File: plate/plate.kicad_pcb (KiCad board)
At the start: 2 copper layers, 134.1 x 128.8 mm, 4 parts

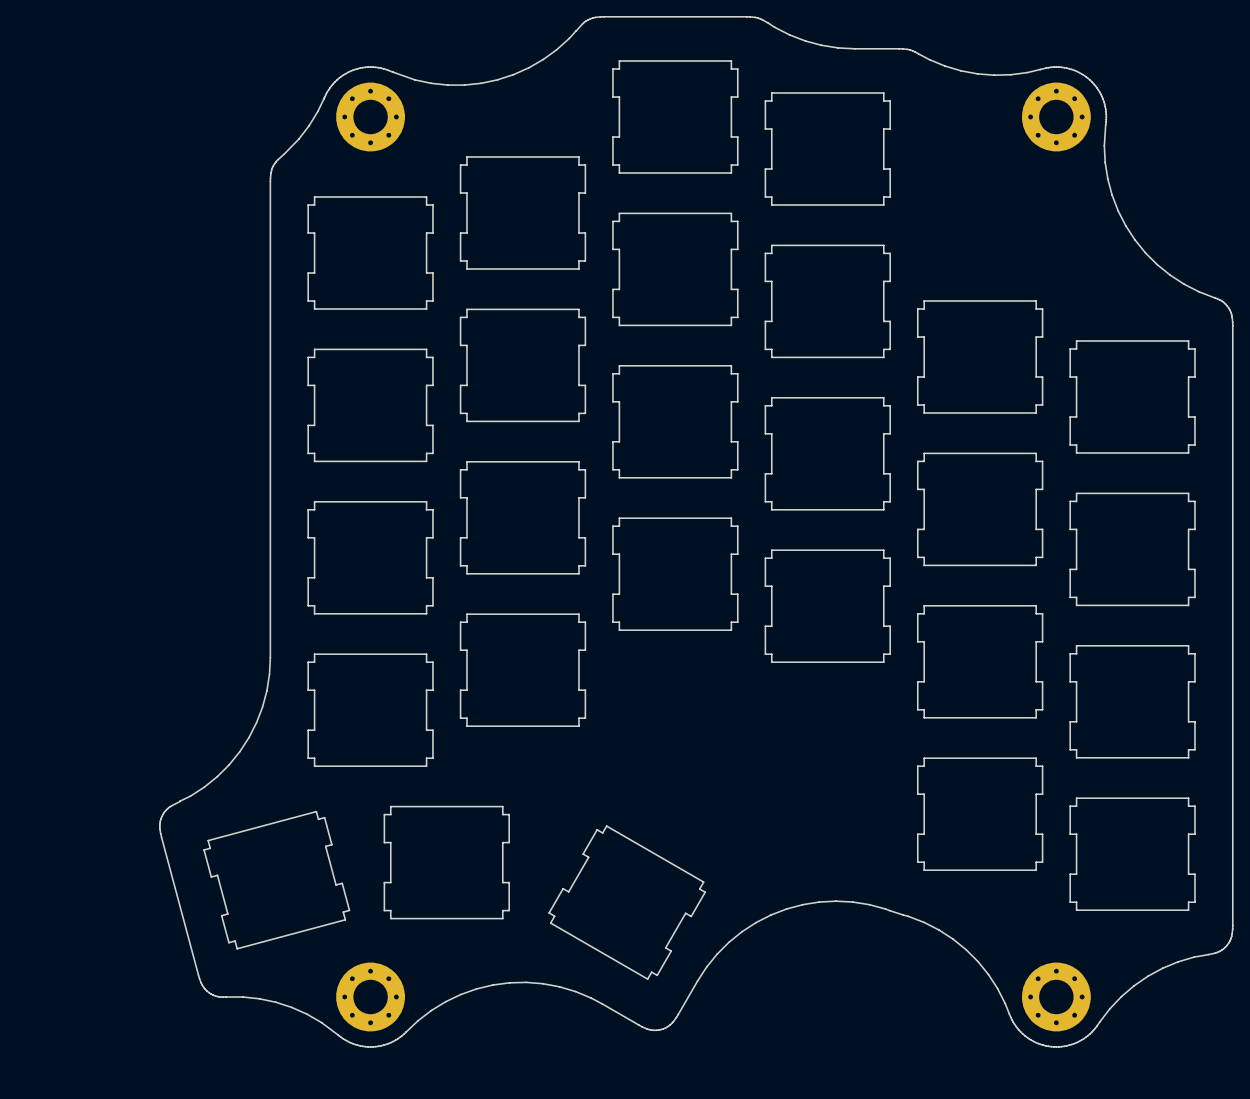
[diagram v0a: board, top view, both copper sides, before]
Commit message: Replace the mounting holes
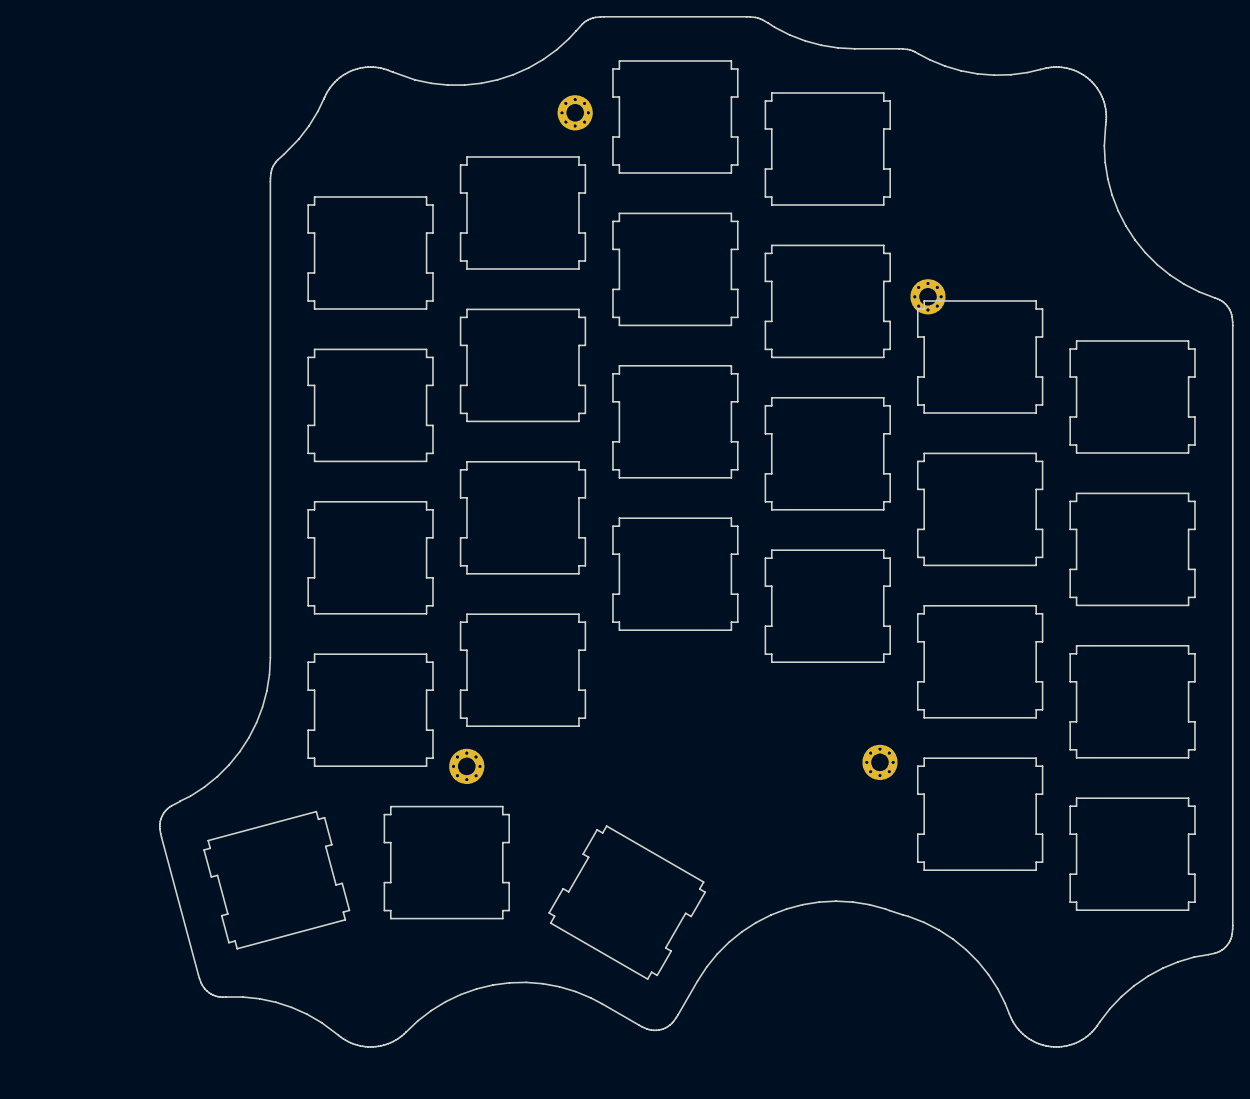
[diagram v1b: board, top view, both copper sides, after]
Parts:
- removed the generated at (85.7, 98.0)
- removed the generated at (85.7, -12.0)
- removed the generated at (0.00, 98.0)
- removed the generated at (0.00, -12.0)
- added generated: MountingHole_2.2mm_M2_Pad_Via, MountingHole_2.2mm_M2_Pad_Via, F.Cu at (25.6, -12.5)
- added generated: MountingHole_2.2mm_M2_Pad_Via, MountingHole_2.2mm_M2_Pad_Via, F.Cu at (69.7, 10.5)
- added generated: MountingHole_2.2mm_M2_Pad_Via, MountingHole_2.2mm_M2_Pad_Via, F.Cu at (12.0, 69.2)
- added generated: MountingHole_2.2mm_M2_Pad_Via, MountingHole_2.2mm_M2_Pad_Via, F.Cu at (63.7, 68.7)

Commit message: Regenerate
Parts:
- added generated: MountingHole_4.3mm_M4_Pad_Via, MountingHole_4.3mm_M4_Pad_Via, F.Cu at (81.7, 98.0)
- added generated: MountingHole_4.3mm_M4_Pad_Via, MountingHole_4.3mm_M4_Pad_Via, F.Cu at (81.7, -12.0)
- added generated: MountingHole_4.3mm_M4_Pad_Via, MountingHole_4.3mm_M4_Pad_Via, F.Cu at (0.00, 98.0)
- added generated: MountingHole_4.3mm_M4_Pad_Via, MountingHole_4.3mm_M4_Pad_Via, F.Cu at (0.00, -12.0)
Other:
- board size 134.1 x 128.8 mm -> 151.6 x 131.1 mm

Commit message: Regenerate plate
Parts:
- removed the generated at (81.7, 98.0)
- removed the generated at (0.00, 98.0)
- removed the generated at (69.7, 10.5)
- removed the generated at (12.0, 69.2)
- added generated: MountingHole_4.3mm_M4_Pad_Via, MountingHole_4.3mm_M4_Pad_Via, F.Cu at (81.7, 94.0)
- added generated: MountingHole_4.3mm_M4_Pad_Via, MountingHole_4.3mm_M4_Pad_Via, F.Cu at (0.00, 94.0)
- added generated: MountingHole_2.2mm_M2_Pad_Via, MountingHole_2.2mm_M2_Pad_Via, F.Cu at (69.7, -8.53)
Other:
- board size 151.6 x 131.1 mm -> 152 x 125.7 mm
